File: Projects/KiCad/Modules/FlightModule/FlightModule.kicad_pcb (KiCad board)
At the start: 2 copper layers, 110 x 95 mm, 67 parts, among them J1 Conn_01x08, J2 Conn_01x02_Pin, J3 Conn_01x02_Pin, J4 Conn_01x02_Pin, J5 Conn_01x02_Pin, J6 Conn_01x02_Pin, Q1 Q_NPN_BEC, SW1 SW_DIP_x02, U1 MCP2562-E-P, U2 NUCLEO-F303K8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

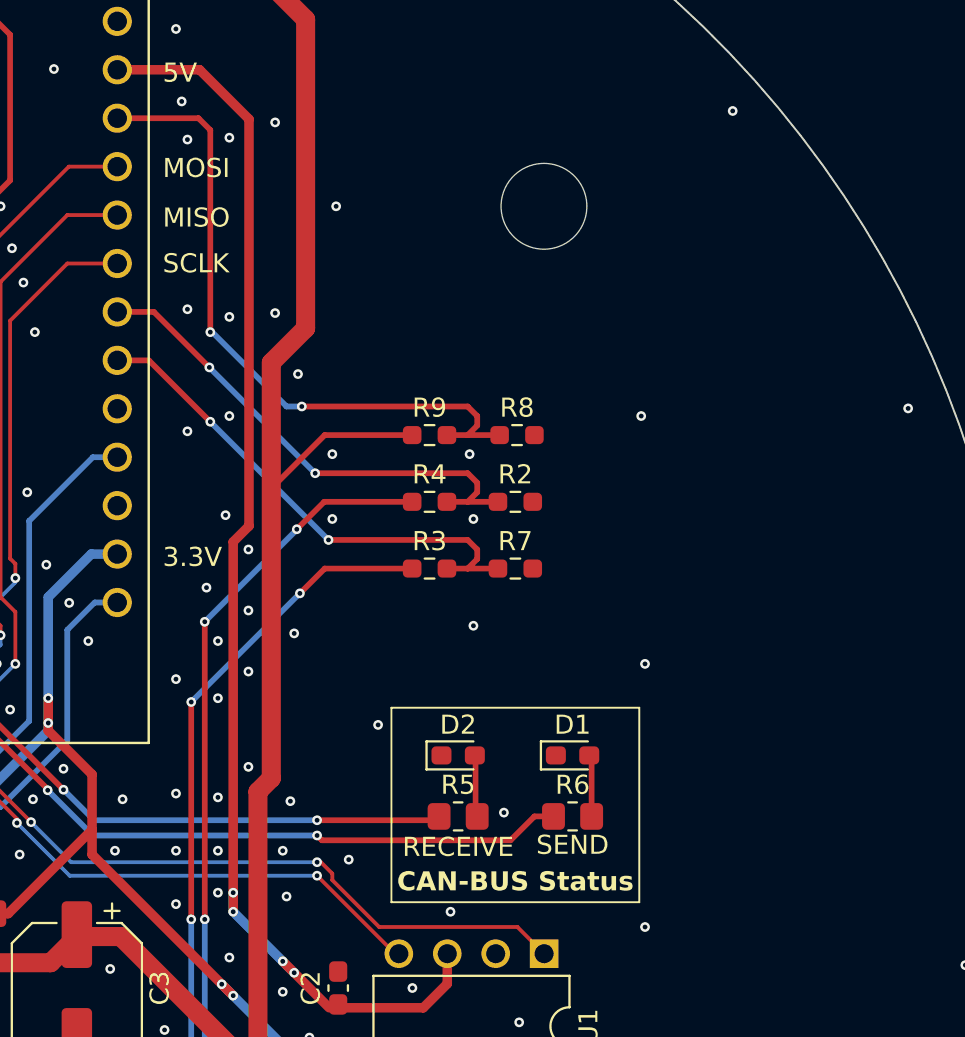
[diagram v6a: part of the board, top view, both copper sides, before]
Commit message: フライトモジュールにブザーを追加
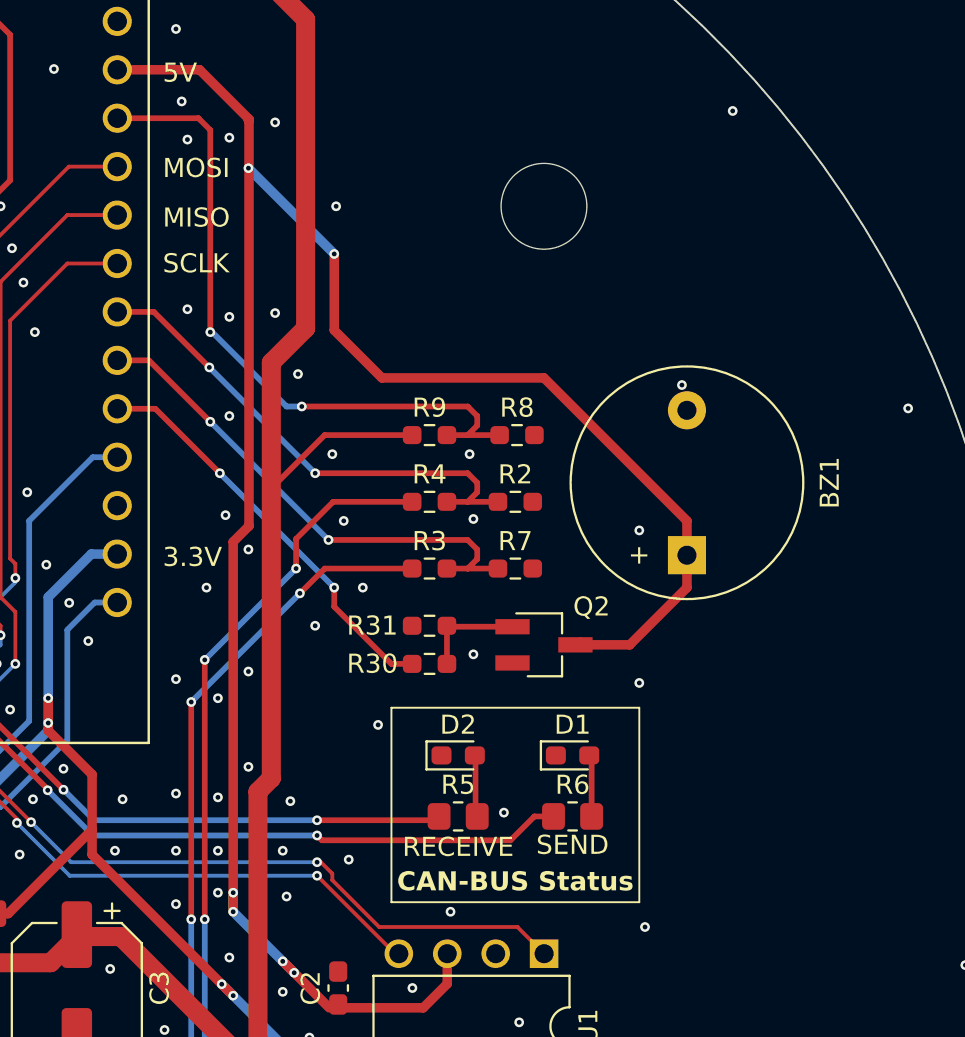
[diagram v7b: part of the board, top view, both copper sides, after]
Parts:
- added BZ1: Buzzer, Buzzer_Beeper:Buzzer_12x9.5RM7.6, F.Cu at (186.0, 93.3)
- added Q2: Q_NPN_BEC, Package_TO_SOT_SMD:SC-59_Handsoldering, F.Cu at (178.5, 98.0)
- added R30: 4.7kΩ, Resistor_SMD:R_0603_1608Metric_Pad0.98x0.95mm_HandSolder, F.Cu at (172.5, 99.0)
- added R31: 4.7kΩ, Resistor_SMD:R_0603_1608Metric_Pad0.98x0.95mm_HandSolder, F.Cu at (172.5, 97.0)
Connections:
- U2 pad 4_11: unconnected-(U2B-PA1-Pad4_11) -> BUZZER
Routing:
- net +5V: track 66.7 -> 110.7 mm, vias 4 -> 6
- net BUZZER: track 0.00 -> 21.6 mm, vias 0 -> 2
- net Net-(Q2-B): track 0.00 -> 5.46 mm
- net GND: vias 184 -> 183

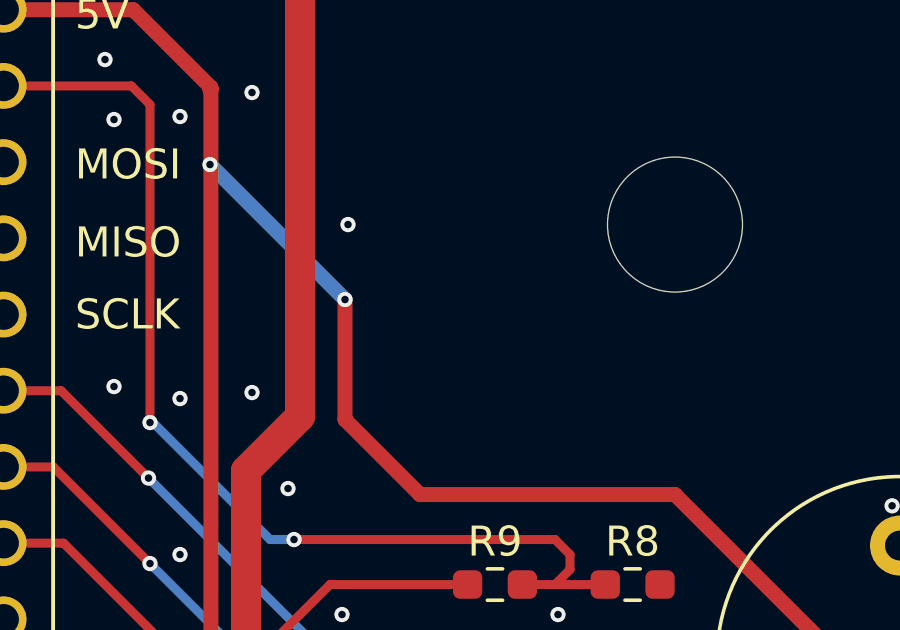
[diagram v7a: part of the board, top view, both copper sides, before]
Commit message: フライトモジュールのGNDにテストポイントを追加
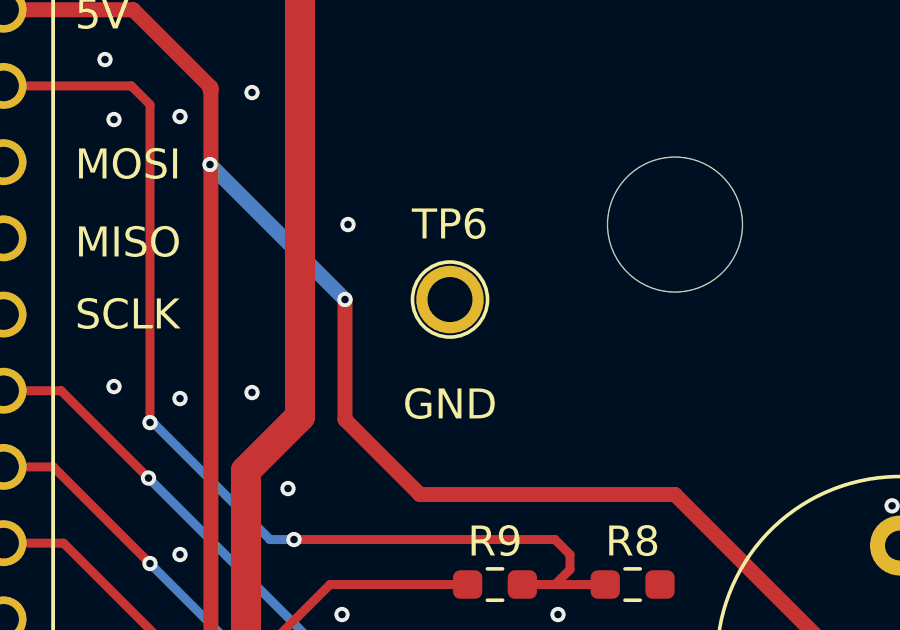
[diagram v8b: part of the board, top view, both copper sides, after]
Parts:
- added TP6: TestPoint, Connector_Pin:Pin_D1.0mm_L10.0mm, F.Cu at (171.0, 77.5)
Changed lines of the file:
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@@
     )
   )
+  (footprint "Connector_Pin:Pin_D1.0mm_L10.0mm" (layer "F.Cu")
+    (at 171 77.5)
+    (descr "solder Pin_ diameter 1.0mm, hole diameter 1.0mm (press fit), length 10.0mm")
+    (tags "solder Pin_ press fit")
+    (property "Sheetfile" "FlightModule.kicad_sch")
+    (property "Sheetname" "")
+    (property "ki_description" "test point")
+    (property "ki_keywords" "test point tp")
+    (attr through_hole)
+    (fp_text reference "TP6" (at 0 -2.5) (layer "F.SilkS")
+        (effects (font (size 1 1) (thickness 0.153)))
+    )
+    (fp_text value "TestPoint" (at 0 -2.05) (layer "F.Fab")
+        (effects (font (size 1 1) (thickness 0.15)))
+    )
+    (fp_text user "${REFERENCE}" (at 0 2.25) (layer "F.Fab")
+        (effects (font (size 1 1) (thickness 0.15)))
+    )
+    (fp_circle (center 0 0) (end 1.25 0.05)
+      (stroke (width 0.12) (type solid)) (fill none) (layer "F.SilkS"))
+    (fp_circle (center 0 0) (end 1.5 0)
+      (stroke (width 0.05) (type solid)) (fill none) (layer "F.CrtYd"))
+    (fp_circle (center 0 0) (end 0.5 0)
+      (stroke (width 0.12) (type solid)) (fill none) (layer "F.Fab"))
+    (fp_circle (center 0 0) (end 1 0)
+      (stroke (width 0.12) (type solid)) (fill none) (layer "F.Fab"))
+    (pad "1" thru_hole circle (at 0 0) (size 2.25 2.25) (drill 1.5) (layers "*.Cu" "*.Mask")
+      (net 2 "GND") (pinfunction "1") (pintype "passive"))
+    (model "${KICAD6_3DMODEL_DIR}/Connector_Pin.3dshapes/Pin_D1.0mm_L10.0mm.wrl"
+      (offset (xyz 0 0 0))
+      (scale (xyz 1 1 1))
+      (rotate (xyz 0 0 0))
+    )
+  )
   (footprint "Resistor_SMD:R_0805_2012Metric_Pad1.20x1.40mm_HandSolder" (layer "F.Cu")
     (at 174 107)
@@
     (effects (font (size 1 1) (thickness 0.2) bold) (justify bottom))
   )
+  (gr_text "GND" (at 171 81) (layer "F.SilkS" knockout)
+    (effects (font (size 1 1) (thickness 0.153)))
+  )
   (gr_text "SEND" (at 180 108.5) (layer "F.SilkS")
